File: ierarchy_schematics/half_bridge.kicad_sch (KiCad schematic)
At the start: 0 parts

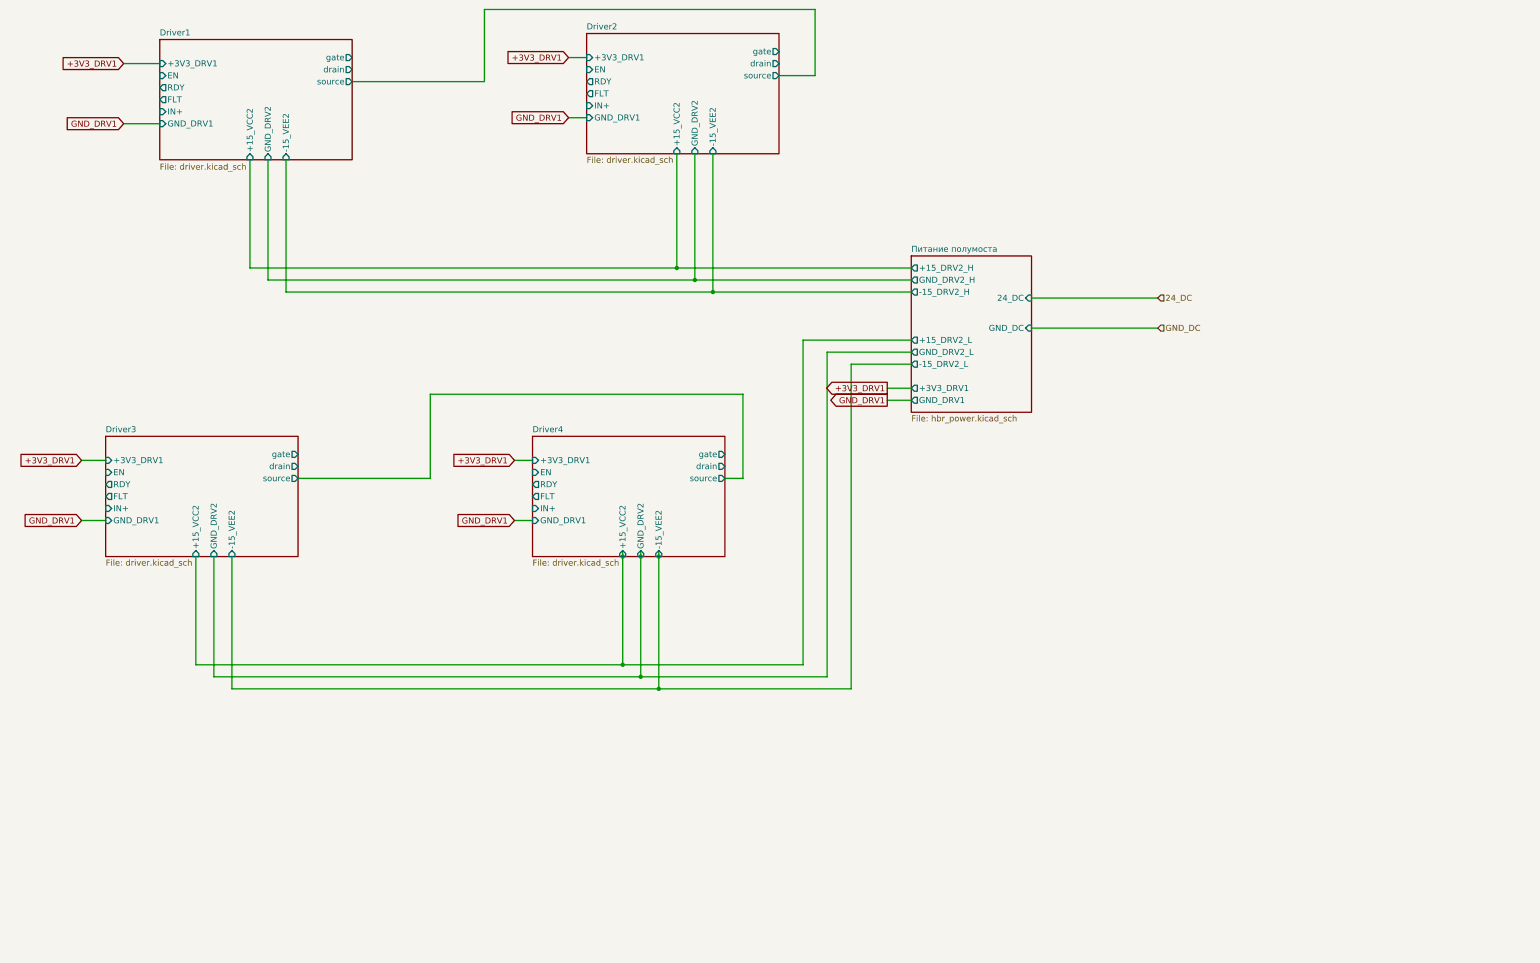
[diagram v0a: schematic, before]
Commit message: Half bridge + power + MCU + optocouplers for one driver.
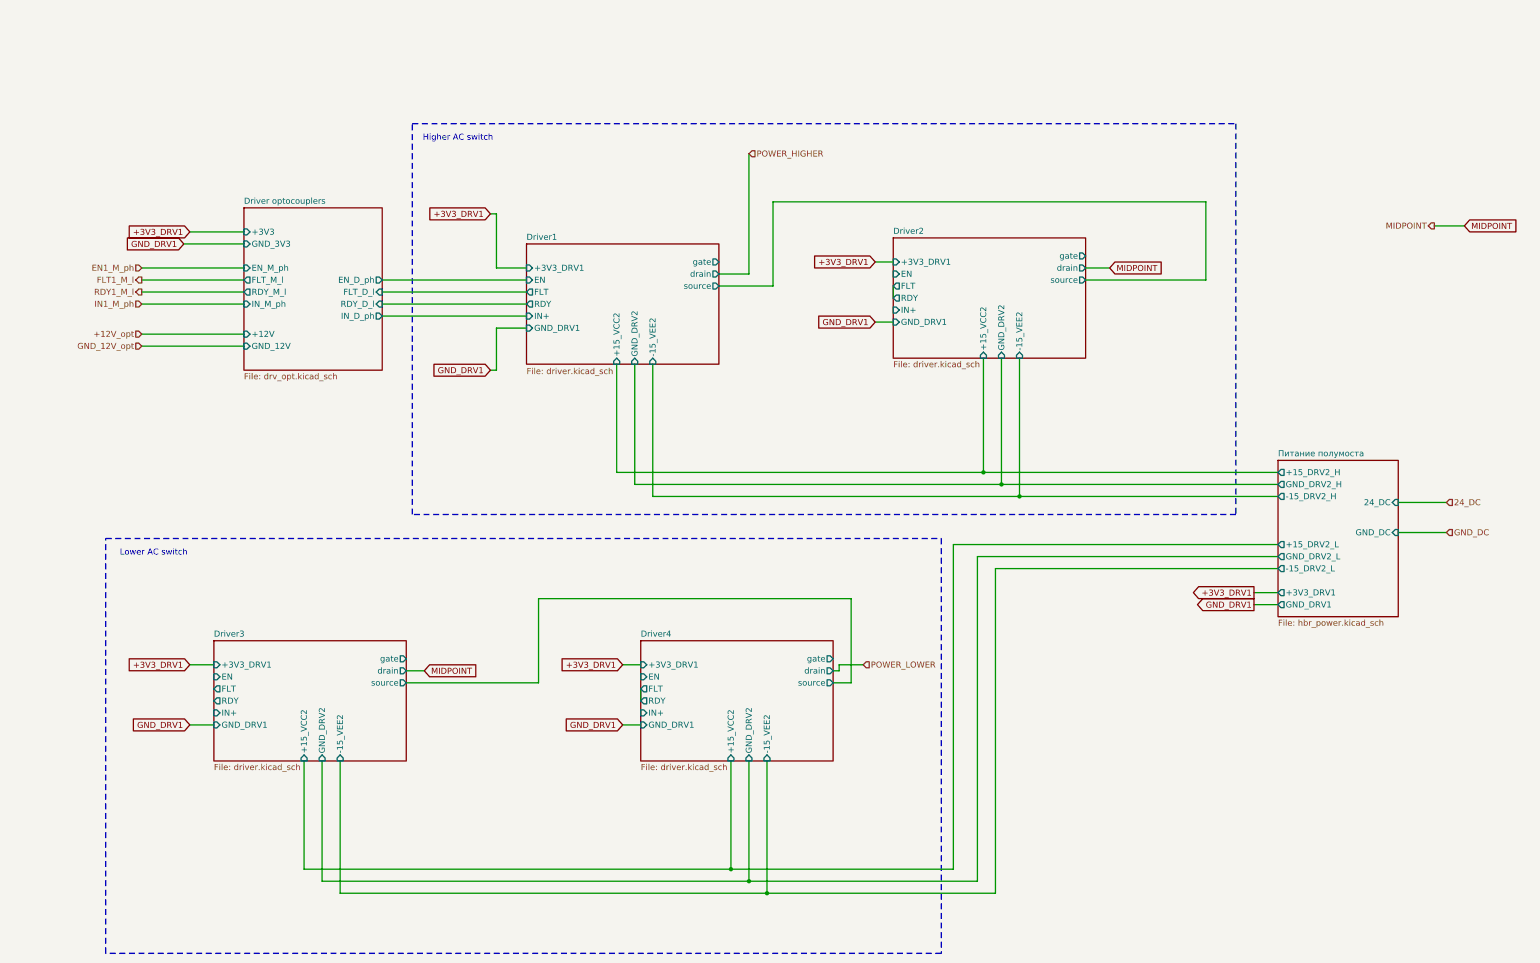
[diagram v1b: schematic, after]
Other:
- added sheet Driver optocouplers (drv_opt.kicad_sch)
- note added: "Higher AC switch"
- note added: "Lower AC switch"
